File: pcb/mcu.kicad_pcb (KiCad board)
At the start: 2 copper layers, 35 x 75 mm, 9 parts, among them J1 N!N, J2 Conn_01x12_Socket, J3 Conn_01x12_Socket, J6 Display_nice-view, SW37 SW_Push, SW38 RotaryEncoder_Switch

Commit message: second draft
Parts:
- added U1: RollerEncoder_EVQWGD001, zzkeeb:RotaryEncoder_EVQWGD001, F.Cu at (73.0, 97.0)
- H5, H6, H7: footprint zzkeeb:Hole_M2-TH -> zzkeeb:Hole_M2-solder-nut-2.5
- moved H7 4.50 mm to (74.0, 107.0)
- moved SW38 3.00 mm to (74.0, 97.0), turned to 180 degrees
- moved J6 1.00 mm to (74.0, 72.0)
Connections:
- J1 pad 20: OFF -> (no net)
- J1 pad 31: encA -> OFF
- J1 pad 32: encB -> (no net)
- J1 pad 33: unconnected-(J1-107-Pad33) -> (no net)
- J1 pad 7: (no net) -> encA
- J1 pad 8: (no net) -> encB
- J2 pad 12: GND -> (no net)
- J2 pad 7: (no net) -> GND
- J3 pad 1: GND -> (no net)
- J3 pad 6: (no net) -> GND
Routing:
- net GND: track 37.5 -> 246.4 mm
- net OFF: track 68.4 -> 52.3 mm
- net (no net): track 415.4 -> 426.2 mm, vias 0 -> 2
- net encA: track 36.6 -> 46.8 mm
- net SCK: track 45.6 -> 41.5 mm
- net +3.3V: track 51.2 -> 47.9 mm
- net encB: track 42.5 -> 40.4 mm
- net MOSI: track 51.7 -> 52.8 mm
- net CS: track 52.6 -> 51.7 mm
- removed copper zone on B.Cu, net GND
- removed copper zone on F.Cu, net GND
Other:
- board size 35 x 75 mm -> 35 x 70.5 mm

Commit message: update case and main pcb
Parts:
- removed U1: RollerEncoder_EVQWGD001, zzkeeb:RotaryEncoder_EVQWGD001
- moved J6 11.5 mm to (74.0, 60.5)
- moved J2 3.50 mm to (70.0, 84.5)
- moved J3 3.50 mm to (78.0, 84.5)
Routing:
- net (no net): track 426.2 -> 482.1 mm
- net MOSI: track 52.8 -> 31.6 mm
- net +3.3V: track 47.9 -> 29.2 mm
- net OFF: track 52.3 -> 37.9 mm
- net CS: track 51.7 -> 37.3 mm, vias 1 -> 0
- net SCK: track 41.5 -> 28.0 mm
- net GND: track 246.4 -> 238.7 mm, vias 1 -> 2
- net encB: track 40.4 -> 35.4 mm
- net encA: track 46.8 -> 43.3 mm
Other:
- outline, holes or cut-outs redrawn
- board text added: "molekula"
- board text added: "v0.2"

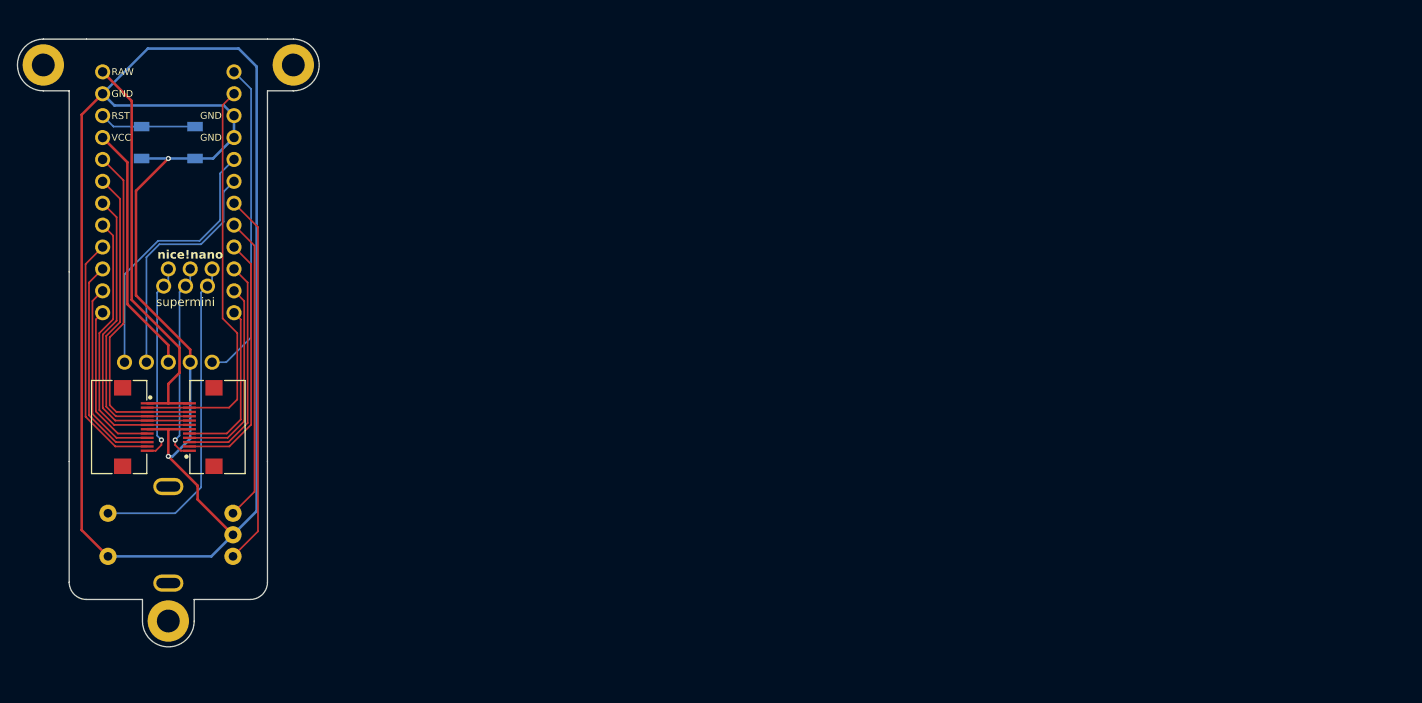
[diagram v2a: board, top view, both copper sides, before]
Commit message: add 3d components
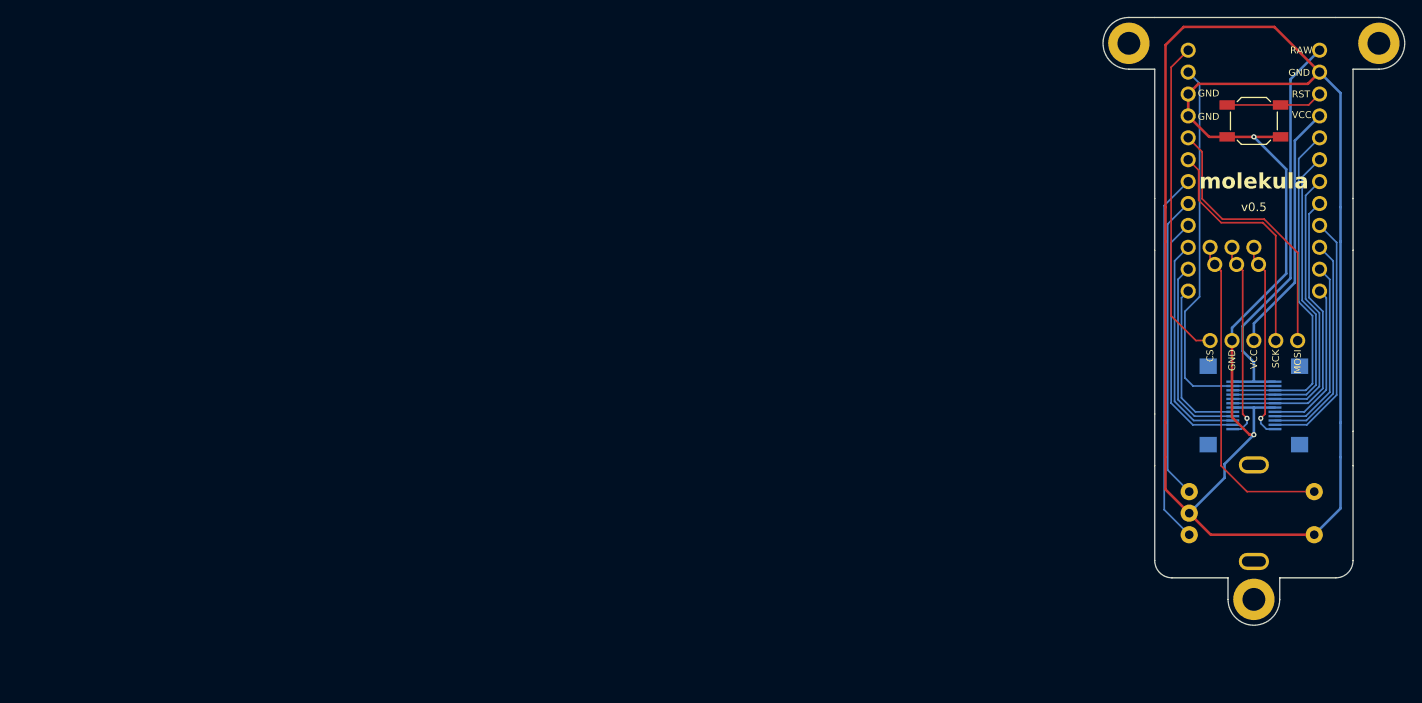
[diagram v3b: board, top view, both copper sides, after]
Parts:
- H5, H6, H7, J6, SW38: moved to B.Cu
- J1, SW37: moved to F.Cu
- J2, J3: value Conn_01x12_Socket -> C479750; moved to B.Cu
- moved H5 154.9 mm to (214.4, 40.0), turned to 180 degrees
- moved J2 133.9 mm to (203.9, 82.0)
- moved H7 125.9 mm to (199.9, 104.5), turned to 180 degrees
- moved J1 125.9 mm to (199.9, 53.5), turned to 0 degrees
- moved J6 125.9 mm to (199.9, 58.0), turned to 180 degrees
- moved SW37 125.9 mm to (199.9, 49.0), turned to 0 degrees
- moved SW38 125.9 mm to (199.9, 94.5), turned to 0 degrees
- moved J3 117.9 mm to (195.9, 82.0)
- moved H6 97.0 mm to (185.4, 40.0), turned to 180 degrees
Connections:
- J1 pad 10: (no net) -> row6-mcu
- J1 pad 11: (no net) -> row5-mcu
- J1 pad 12: (no net) -> row4-mcu
- J1 pad 13: (no net) -> row3-mcu
- J1 pad 14: (no net) -> row2-mcu
- J1 pad 15: (no net) -> row1-mcu
- J1 pad 16: (no net) -> row0-mcu
- J1 pad 17: (no net) -> col0-mcu
- J1 pad 18: (no net) -> col1-mcu
- J1 pad 19: (no net) -> col2-mcu
- J1 pad 2: (no net) -> col4-mcu
- J1 pad 20: (no net) -> col3-mcu
- J1 pad 24: (no net) -> BAT-mcu
- J1 pad 32: (no net) -> free2-mcu
- J1 pad 33: (no net) -> free1-mcu
- J1 pad 9: (no net) -> row7-mcu
- J2 pad 1: (no net) -> BAT-mcu
- J2 pad 10: (no net) -> row1-mcu
- J2 pad 11: (no net) -> row0-mcu
- J2 pad 12: (no net) -> free1-mcu
- J2 pad 2: (no net) -> col4-mcu
- J2 pad 3: (no net) -> col3-mcu
- J2 pad 4: (no net) -> col2-mcu
- J2 pad 5: (no net) -> col1-mcu
- J2 pad 6: (no net) -> col0-mcu
- J2 pad 8: (no net) -> row3-mcu
- J2 pad 9: (no net) -> row2-mcu
- J3 pad 1: (no net) -> free2-mcu
- J3 pad 10: (no net) -> col3-mcu
- J3 pad 11: (no net) -> col4-mcu
- J3 pad 12: (no net) -> BAT-mcu
- J3 pad 2: (no net) -> row7-mcu
- J3 pad 3: (no net) -> row6-mcu
- J3 pad 4: (no net) -> row5-mcu
- J3 pad 5: (no net) -> row4-mcu
- J3 pad 7: (no net) -> col0-mcu
- J3 pad 8: (no net) -> col1-mcu
- J3 pad 9: (no net) -> col2-mcu
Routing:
- net (no net): track 482.1 -> 0.00 mm, vias 2 -> 0
- net BAT-mcu: track 0.00 -> 47.6 mm
- net col4-mcu: track 0.00 -> 47.6 mm
- net col3-mcu: track 0.00 -> 39.7 mm
- net col2-mcu: track 0.00 -> 37.7 mm
- net col1-mcu: track 0.00 -> 35.7 mm
- net col0-mcu: track 0.00 -> 33.8 mm
- net row7-mcu: track 0.00 -> 29.6 mm
- net row0-mcu: track 0.00 -> 29.1 mm
- net row6-mcu: track 0.00 -> 26.2 mm
- net row1-mcu: track 0.00 -> 25.7 mm
- net free1-mcu: track 0.00 -> 23.1 mm, vias 0 -> 1
- net free2-mcu: track 0.00 -> 23.1 mm, vias 0 -> 1
- net row5-mcu: track 0.00 -> 22.8 mm
- net row2-mcu: track 0.00 -> 22.3 mm
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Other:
- outline, holes or cut-outs redrawn
- board text added: "v0.5"
- board text removed: "v0.2"
